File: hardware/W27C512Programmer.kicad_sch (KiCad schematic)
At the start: 76 parts, among them J1 CTRL, J2 MSB, J3 LSB, J4 Ext_UART, Q1 2N3904, Q2 2N3906, Q3 2N3904, Q4 2N3904, Q5 2N3904, Q6 2N3906, Q7 2N3906, Q8 2N3906, U1 MIC2288, U2 74HC573, U3 74HC573, U4 74HC573, U5 28/32 pin ROM

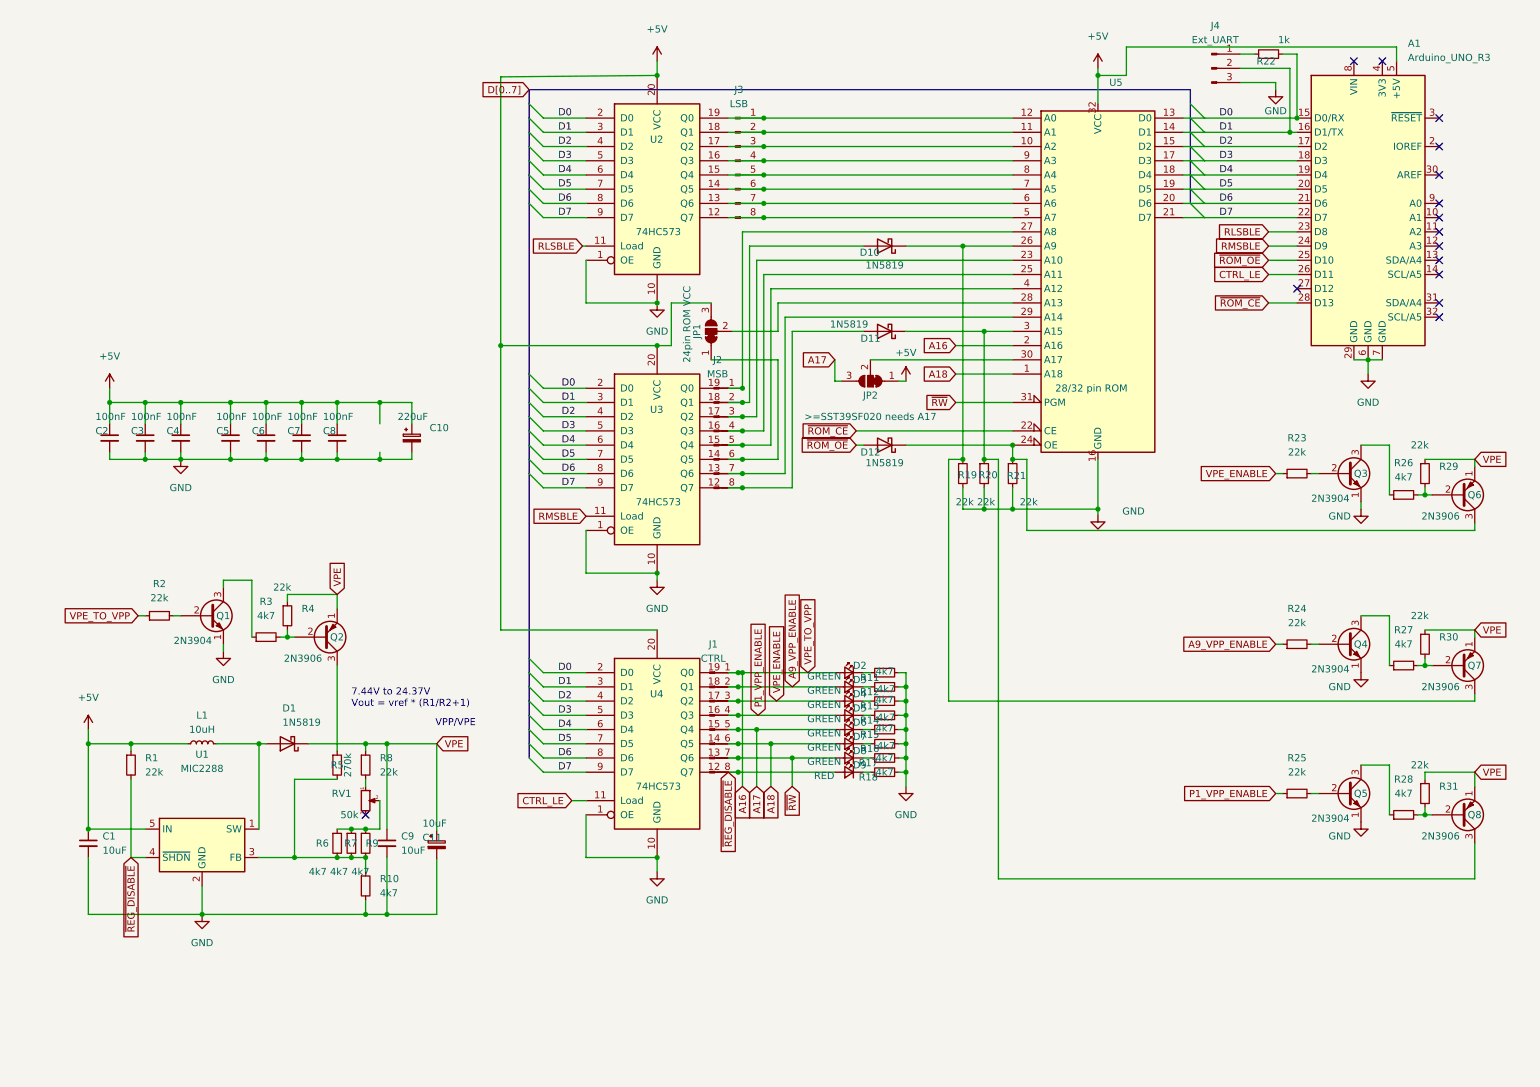
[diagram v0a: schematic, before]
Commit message: PCB probably somewhat complete
Completely untested PCB. Maybe it works. Maybe I should look for someone to review...
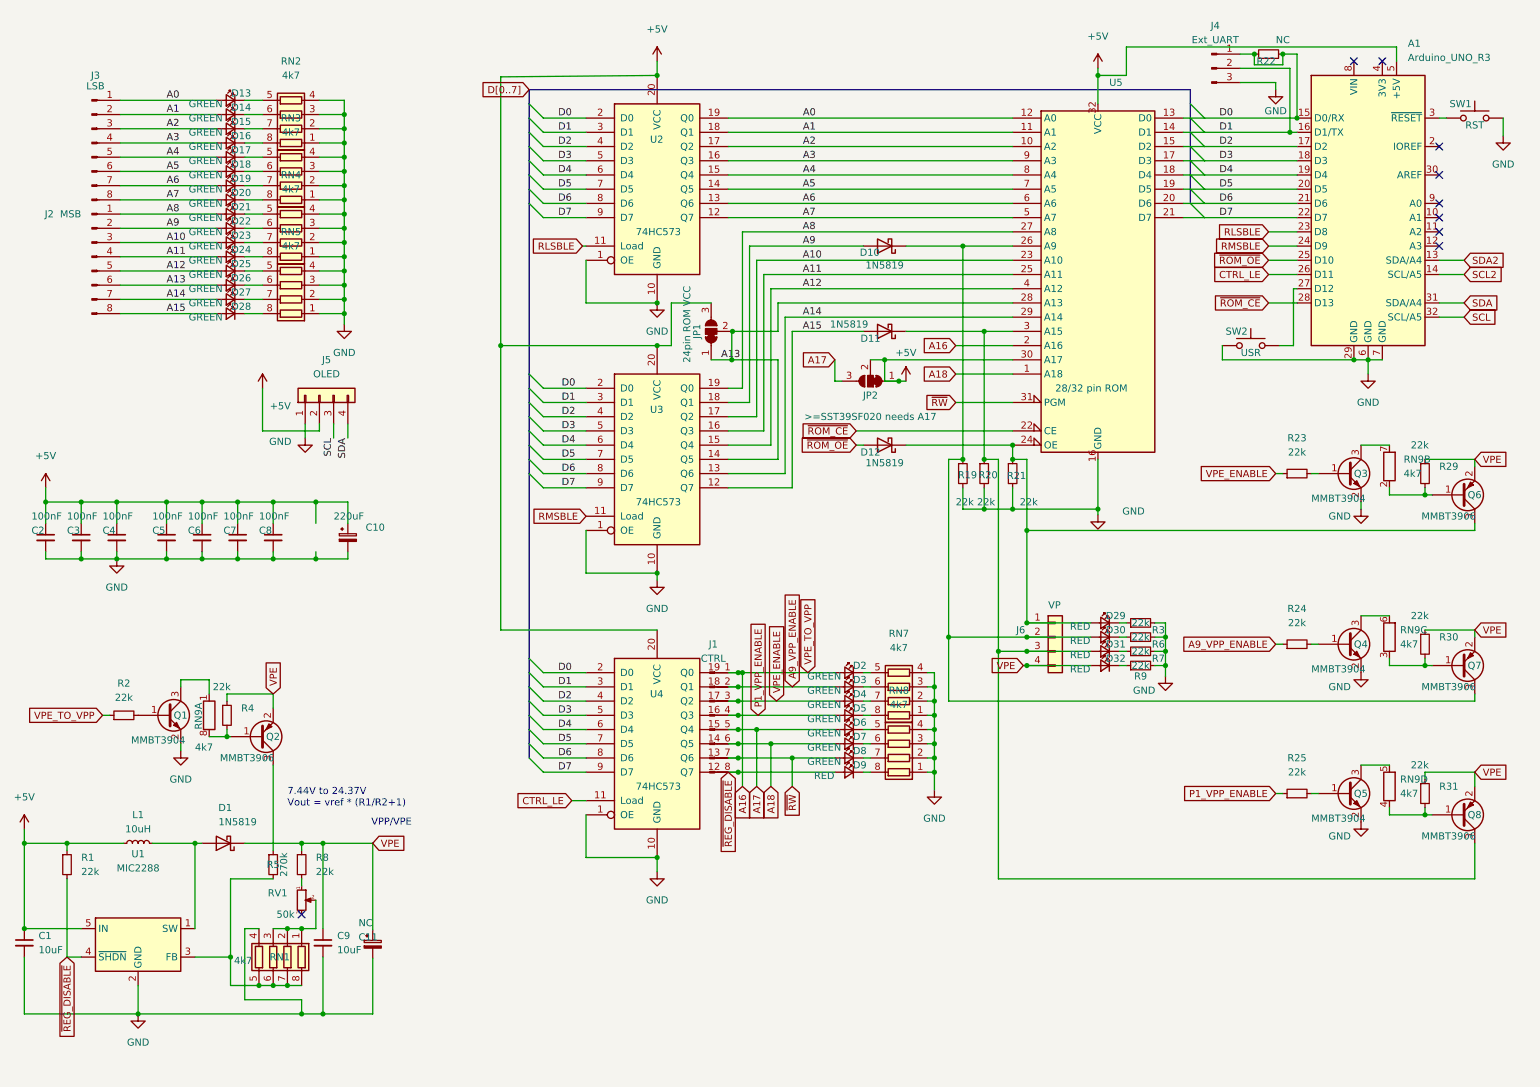
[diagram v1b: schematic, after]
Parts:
- removed R10, R11, R12, R13, R14, R15, R16, R17, R18, R26, R27, R28: 4k7, Resistor_SMD:R_0603_1608Metric, symbol Device:R_Small
- added D13, D14, D15, D16, D17, D18, D19, D20, D21, D22, D23, D24, D25, D26, D27, D28: GREEN, LED_SMD:LED_0805_2012Metric, symbol Device:LED_Small
- added D29, D30, D31, D32: RED, LED_SMD:LED_0603_1608Metric, symbol Device:LED_Small
- added J5: OLED, Connector_PinSocket_2.54mm:PinSocket_1x04_P2.54mm_Vertical, symbol Connector_Generic:Conn_01x04
- added J6: VP, Connector_PinSocket_2.54mm:PinSocket_1x04_P2.54mm_Vertical, symbol Connector_Generic:Conn_01x04
- added RN1, RN2, RN3, RN4, RN5, RN7, RN8: 4k7, Resistor_SMD:R_Array_Convex_4x0603, symbol Device:R_Pack04
- added RN9: 4k7, Resistor_SMD:R_Array_Convex_4x0603, symbol Device:R_Pack04_Split
- added SW1: RST, Button_Switch_SMD:SW_SPST_TL3342, symbol Switch:SW_Push
- added SW2: USR, Button_Switch_SMD:SW_SPST_TL3342, symbol Switch:SW_Push
- A1: now left out of the parts list
- C1, C9: LCSC (none) -> C13585
- C11: value 10uF -> NC
- D1, D10, D11, D12: footprint Diode_SMD:D_SOD-123 -> Diode_SMD:D_SOD-323; LCSC (none) -> C191023
- D2, D3, D4, D5, D6, D7, D8: footprint LED_SMD:LED_0603_1608Metric -> LED_SMD:LED_0805_2012Metric
- L1: footprint Inductor_SMD:L_0805_2012Metric -> Inductor_SMD:L_Taiyo-Yuden_MD-4040; LCSC (none) -> C497774
- Q1, Q3, Q4, Q5: value 2N3904 -> MMBT3904; symbol Transistor_BJT:2N3904 -> Transistor_BJT:MMBT3904
- Q2, Q6, Q7, Q8: value 2N3906 -> MMBT3906; symbol Transistor_BJT:2N3906 -> Transistor_BJT:MMBT3906
- R22: value 1k -> NC
- R3, R6, R7, R9: value 4k7 -> 22k
- RV1: LCSC (none) -> C913246
- U1: LCSC (none) -> C181783
- U2, U3, U4: LCSC (none) -> C3151971
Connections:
- net +5V: now also JP2.2 (C), U5.30 (A17), J5.2 (Pin_2)
- net D0: now also J4.1 (Pin_1), R22.1
- net GND: now also Q1.2 (E), Q3.2 (E), Q4.2 (E), Q5.2 (E), R3.2, R6.2, R7.2, R9.2, J5.1 (Pin_1), RN1.4 (R4.1), RN2.1 (R1.1), RN2.2 (R2.1), RN2.3 (R3.1), RN2.4 (R4.1), RN3.1 (R1.1), RN3.2 (R2.1), RN3.3 (R3.1), RN3.4 (R4.1), RN4.1 (R1.1), RN4.2 (R2.1), RN4.3 (R3.1), RN4.4 (R4.1), RN5.1 (R1.1), RN5.2 (R2.1), RN5.3 (R3.1), RN5.4 (R4.1), RN7.1 (R1.1), RN7.2 (R2.1), RN7.3 (R3.1), RN7.4 (R4.1), RN8.1 (R1.1), RN8.2 (R2.1), RN8.3 (R3.1), RN8.4 (R4.1), SW1.2, SW2.1; no longer Q1.1 (E), Q3.1 (E), Q4.1 (E), Q5.1 (E)
- net VPE: now also Q2.2 (E), Q6.2 (E), Q7.2 (E), Q8.2 (E), D32.2 (A), J6.4 (Pin_4); no longer Q2.1 (E), Q6.1 (E), Q7.1 (E), Q8.1 (E)
- net at D11.1 (K), Q8.3 (C), R20.1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: now also D31.2 (A), J6.3 (Pin_3)
- net A15: now reaches D11.2 (A), J2.8 (Pin_8), U3.12 (Q7)
- net A15: now also D28.2 (A)
- net at D2.1 (K): now also RN7.5 (R4.2)
- net at R24.2: now also Q4.1 (B); no longer Q4.2 (B)
- net at D7.1 (K): now also RN8.6 (R3.2)
- net at R2.2: now also Q1.1 (B); no longer Q1.2 (B)
- net at Q1.3 (C): now also RN9.1 (R1.1); no longer R3.1
- net at R25.2: now also Q5.1 (B); no longer Q5.2 (B)
- net at R30.2: now also Q7.1 (B), RN9.3 (R3.1); no longer Q7.2 (B)
- net at D9.1 (K): now also RN8.8 (R1.2)
- net at D5.1 (K): now also RN7.8 (R1.2)
- net at Q4.3 (C): now also RN9.6 (R3.2)
- net A8: now reaches J2.1 (Pin_1), U3.19 (Q0), U5.27 (A8)
- net A8: now also D21.2 (A)
- net A9: now reaches D10.2 (A), J2.2 (Pin_2), U3.18 (Q1)
- net A9: now also D22.2 (A)
- net A10: now reaches J2.3 (Pin_3), U3.17 (Q2), U5.23 (A10)
- net A10: now also D23.2 (A)
- net A11: now reaches J2.4 (Pin_4), U3.16 (Q3), U5.25 (A11)
- net A11: now also D24.2 (A)
- net A12: now reaches J2.5 (Pin_5), U3.15 (Q4), U5.4 (A12)
- net A12: now also D25.2 (A)
- net A13: now reaches J2.6 (Pin_6), JP1.1 (A), U3.14 (Q5)
- net A13: now also JP1.2 (C), U5.28 (A13), D26.2 (A)
- net A14: now reaches J2.7 (Pin_7), U3.13 (Q6), U5.29 (A14)
- net A14: now also D27.2 (A)
- net A0: now reaches J3.1 (Pin_1), U2.19 (Q0), U5.12 (A0)
- net A0: now also D13.2 (A)
- net A1: now reaches J3.2 (Pin_2), U2.18 (Q1), U5.11 (A1)
- net A1: now also D14.2 (A)
- net A2: now reaches J3.3 (Pin_3), U2.17 (Q2), U5.10 (A2)
- net A2: now also D15.2 (A)
- net A3: now reaches J3.4 (Pin_4), U2.16 (Q3), U5.9 (A3)
- net A3: now also D16.2 (A)
- net A4: now reaches J3.5 (Pin_5), U2.15 (Q4), U5.8 (A4)
- net A4: now also D17.2 (A)
- net A5: now reaches J3.6 (Pin_6), U2.14 (Q5), U5.7 (A5)
- net A5: now also D18.2 (A)
- net A6: now reaches J3.7 (Pin_7), U2.13 (Q6), U5.6 (A6)
- net A6: now also D19.2 (A)
- net A7: now reaches J3.8 (Pin_8), U2.12 (Q7), U5.5 (A7)
- net A7: now also D20.2 (A)
- net at D6.1 (K): now also RN8.5 (R4.2)
- net at D8.1 (K): now also RN8.7 (R2.2)
- net at D10.1 (K), Q7.3 (C), R19.1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: now also D30.2 (A), J6.2 (Pin_2)
- net at R31.2: now also Q8.1 (B), RN9.4 (R4.1); no longer Q8.2 (B)
- net at D3.1 (K): now also RN7.6 (R3.2)
- net at D4.1 (K): now also RN7.7 (R2.2)
- net at Q3.3 (C): now also RN9.7 (R2.2)
- net at R29.2: now also Q6.1 (B), RN9.2 (R2.1); no longer Q6.2 (B)
- net at D12.1 (K), Q6.3 (C), R21.1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: now also D29.2 (A), J6.1 (Pin_1)
- net at Q5.3 (C): now also RN9.5 (R4.2)
- net at R23.2: now also Q3.1 (B); no longer Q3.2 (B)
- net SDA2: now reaches A1.13 (SDA/A4)
- net SCL2: now reaches A1.14 (SCL/A5)
- net at A1.27 (D12): now also SW2.2
- net at A1.3 (~{RESET}): now also SW1.1
- net SDA: now reaches A1.31 (SDA/A4)
- net SDA: now also J5.4 (Pin_4)
- net SCL: now reaches A1.32 (SCL/A5)
- net SCL: now also J5.3 (Pin_3)
- new net: D25.1 (K), RN5.5 (R4.2)
- new net: D26.1 (K), RN5.6 (R3.2)
- new net: D27.1 (K), RN5.7 (R2.2)
- new net: D28.1 (K), RN5.8 (R1.2)
- new net: D31.1 (K), R7.1
- new net: D32.1 (K), R9.1
- new net: D20.1 (K), RN3.8 (R1.2)
- new net: D16.1 (K), RN2.8 (R1.2)
- new net: Q2.1 (B), R4.2, RN9.8 (R1.2)
- new net: D21.1 (K), RN4.5 (R4.2)
- new net: R5.2, RN1.5 (R4.2), RN1.6 (R3.2), RN1.7 (R2.2), RN1.8 (R1.2), U1.3 (FB)
- new net: D13.1 (K), RN2.5 (R4.2)
- new net: D14.1 (K), RN2.6 (R3.2)
- new net: D15.1 (K), RN2.7 (R2.2)
- new net: D17.1 (K), RN3.5 (R4.2)
- new net: RN1.1 (R1.1), RN1.2 (R2.1), RN1.3 (R3.1), RV1.2
- new net: D23.1 (K), RN4.7 (R2.2)
- new net: D29.1 (K), R3.1
- new net: D22.1 (K), RN4.6 (R3.2)
- new net: D24.1 (K), RN4.8 (R1.2)
- new net: D19.1 (K), RN3.7 (R2.2)
- new net: D30.1 (K), R6.1
- new net: D18.1 (K), RN3.6 (R3.2)
- no-connect marks 15 -> 9
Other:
- moved on the sheet: C1, C10, C11, C2, C3, C4, C5, C6, C7, C8, C9, D1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

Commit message: Hardware release day update!
Gerber files (zip) BOM, placement and KiCAD files as they are for Rev0
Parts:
- removed R22: NC, Resistor_SMD:R_0603_1608Metric, symbol Device:R_Small
- added D33: 1N5819, Diode_SMD:D_SOD-323, symbol Diode:1N5819
- added J7: SAO, Connector_PinHeader_2.54mm:PinHeader_2x03_P2.54mm_Vertical, symbol Connector_Generic:Conn_02x03_Odd_Even
- added JP3: W27C010/AT27C010 needs p1 VPE/VPP (32 pin), Jumper:SolderJumper-3_P1.3mm_Open_RoundedPad1.0x1.5mm, symbol Jumper:Jumper_3_Open
- added R10, R11: 1k, Resistor_SMD:R_0603_1608Metric, symbol Device:R_Small
- added R12: 22k, Resistor_SMD:R_0603_1608Metric, symbol Device:R_Small
- C10: LCSC (none) -> C131120
- D13, D14, D15, D16, D17, D18, D19, D2, D20, D21, D22, D23, D24, D25, D26, D27, D28, D3, D4, D5, D6, D7, D8: LCSC (none) -> C2297
- JP1: footprint Connector_PinHeader_2.54mm:PinHeader_1x03_P2.54mm_Vertical -> Connector_PinHeader_2.54mm:PinHeader_1x03_P2.54mm_Vertical_SolderJumpers; symbol Jumper:SolderJumper_3_Bridged12 -> Jumper:Jumper_3_Open
- JP2: value >=SST39SF020 needs A17 -> >=SST39SF020 & 28C512 need A17; footprint Connector_PinHeader_2.54mm:PinHeader_1x03_P2.54mm_Vertical -> Connector_PinHeader_2.54mm:PinHeader_1x03_P2.54mm_Vertical_SolderJumpers; symbol Jumper:SolderJumper_3_Bridged12 -> Jumper:Jumper_3_Open
- Q1, Q3, Q4, Q5: LCSC (none) -> C20526
- Q2, Q6, Q7, Q8: LCSC (none) -> C7420354
- RN1, RN2, RN3, RN4, RN5, RN7, RN8, RN9: LCSC (none) -> C1980
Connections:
- net +5V: no longer JP2.2 (C), U5.30 (A17)
- net A13: no longer JP1.2 (C), U5.28 (A13)
- net A18: now also D33.2 (A); no longer U5.1 (A18)
- net D0: now also R10.2; no longer J4.1 (Pin_1)
- net D1: now also R11.2; no longer J4.2 (Pin_2)
- net GND: now also RN1.5 (R4.2), J7.2 (Pin_2), R12.2; no longer RN1.4 (R4.1)
- net SCL2: now also J7.4 (Pin_4)
- net SDA2: now also J7.3 (Pin_3)
- net at D11.1 (K), R20.1, U5.3 (A15): now also JP3.1 (A); no longer D31.2 (A), J6.3 (Pin_3), Q8.3 (C)
- net at RN1.6 (R3.2), RN1.7 (R2.2), RN1.8 (R1.2): no longer R5.2, RN1.5 (R4.2), U1.3 (FB)
- net at RN1.1 (R1.1), RN1.2 (R2.1), RV1.2: no longer RN1.3 (R3.1)
- net at A1.10 (A1): now also J7.6 (Pin_6)
- net at A1.4 (3V3): now also J7.1 (Pin_1)
- net at A1.9 (A0): now also J7.5 (Pin_5)
- new net: D31.2 (A), J6.3 (Pin_3), JP3.2 (C), Q8.3 (C)
- new net: J4.2 (Pin_2), R11.1
- new net: R5.2, RN1.3 (R3.1), RN1.4 (R4.1), U1.3 (FB)
- new net: J4.1 (Pin_1), R10.1
- new net: D33.1 (K), JP3.3 (B), R12.1, U5.1 (A18)
- new net: JP1.2 (C), U5.28 (A13)
- new net: JP2.2 (C), U5.30 (A17)
- no-connect marks 9 -> 6
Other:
- note added: "8.83V to 21.92V Vout = vref * (R1/R2+1)"
- note added: "vref = 1.23 "R1" = R8 + RV1 + partial RN1 (2350+4700) "R2" = partial RN1 (4700) VPE-Max = 1.23 * ((22000+50000+2350+4700)/4700+1) == 21.92V VPE-Min = 1.23 * ((22000+0+2350+4700)/4700+1) == 8.83V"
- note removed: "7.44V to 24.37V Vout = vref * (R1/R2+1)"
- moved on the sheet: D11, D12

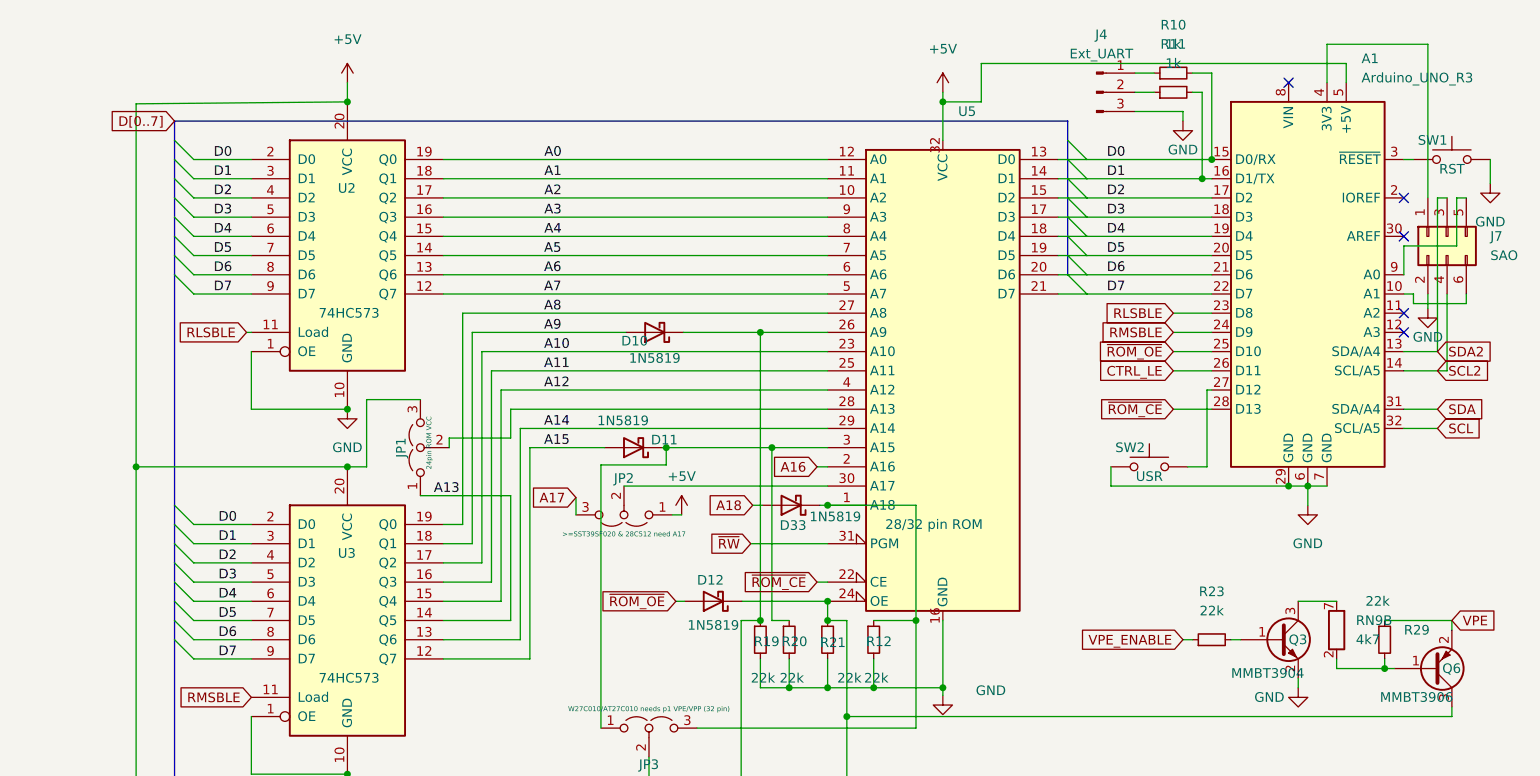
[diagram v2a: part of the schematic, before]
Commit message: Rev1 PCB - Includes voltage divider on Arduino Analog Pin 2.
Voltage divider on Arduino Analog Pin 2 as well as updated LCSC part numbers.. So you don't end up getting the wrong color LEDs.
Remember to use the Rev1b0 gerber zip file and not Rev0.
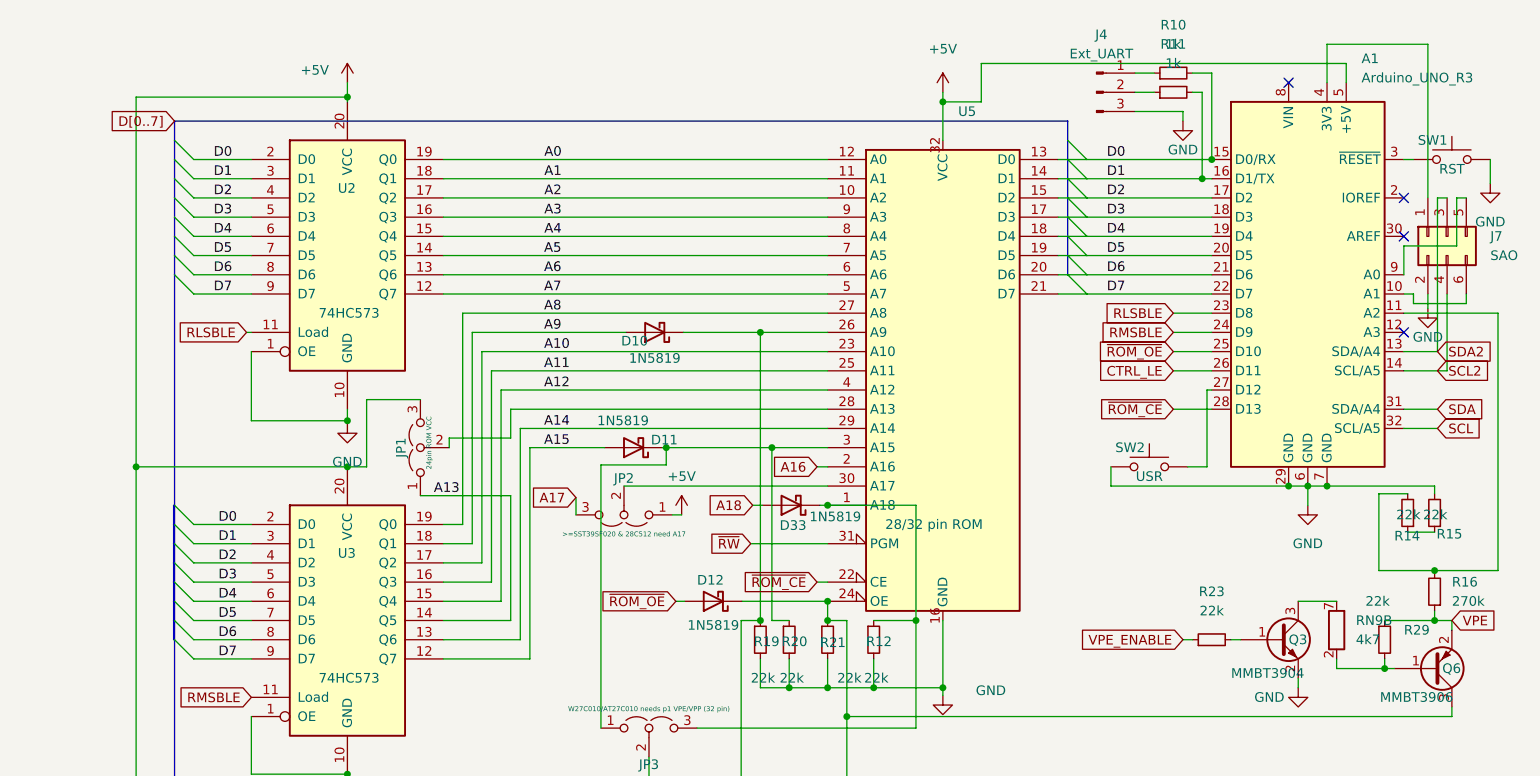
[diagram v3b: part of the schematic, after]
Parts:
- added R14, R15: 22k, Resistor_SMD:R_0603_1608Metric, symbol Device:R_Small
- added R16: 270k, Resistor_SMD:R_0603_1608Metric, symbol Device:R_Small
- D29, D30, D31, D32, D9: LCSC (none) -> C2286
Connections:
- net GND: now also R15.2
- net VPE: now also R16.1
- net at A1.11 (A2): now also R14.2, R16.2
- new net: R14.1, R15.1
- no-connect marks 6 -> 5
